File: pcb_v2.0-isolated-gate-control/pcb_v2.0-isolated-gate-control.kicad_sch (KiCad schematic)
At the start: 94 parts, among them J1 ServoLock, J10 Buttons, J11 2x encoder, J12 Screw_Terminal_01x06, J13 Relay VFD2 [NO, COM, NC], J14 GND-P, J15 Power-Servo-12V, J16 Power-LightBarrier-12V, J17 3V3 5V VDD, J18 GNDD, J2 supply, J3 12V-filtered, J4 light-barrier, reserve, J5 GND-P, J6 2x remoteControl, J7 Relay VFD1 [NO, COM, NC], J8 RS485, J9 limit, K1 RT314A24, K2 RT314A24, Q1 2N7000, Q2 2N7000, Q3 IRF5305, Q6 IRF5305, U1 esp32-devkit-v1_30Pin, U4 MAX485E, U5 L78S05CV_TO220, U6 ULN2803A

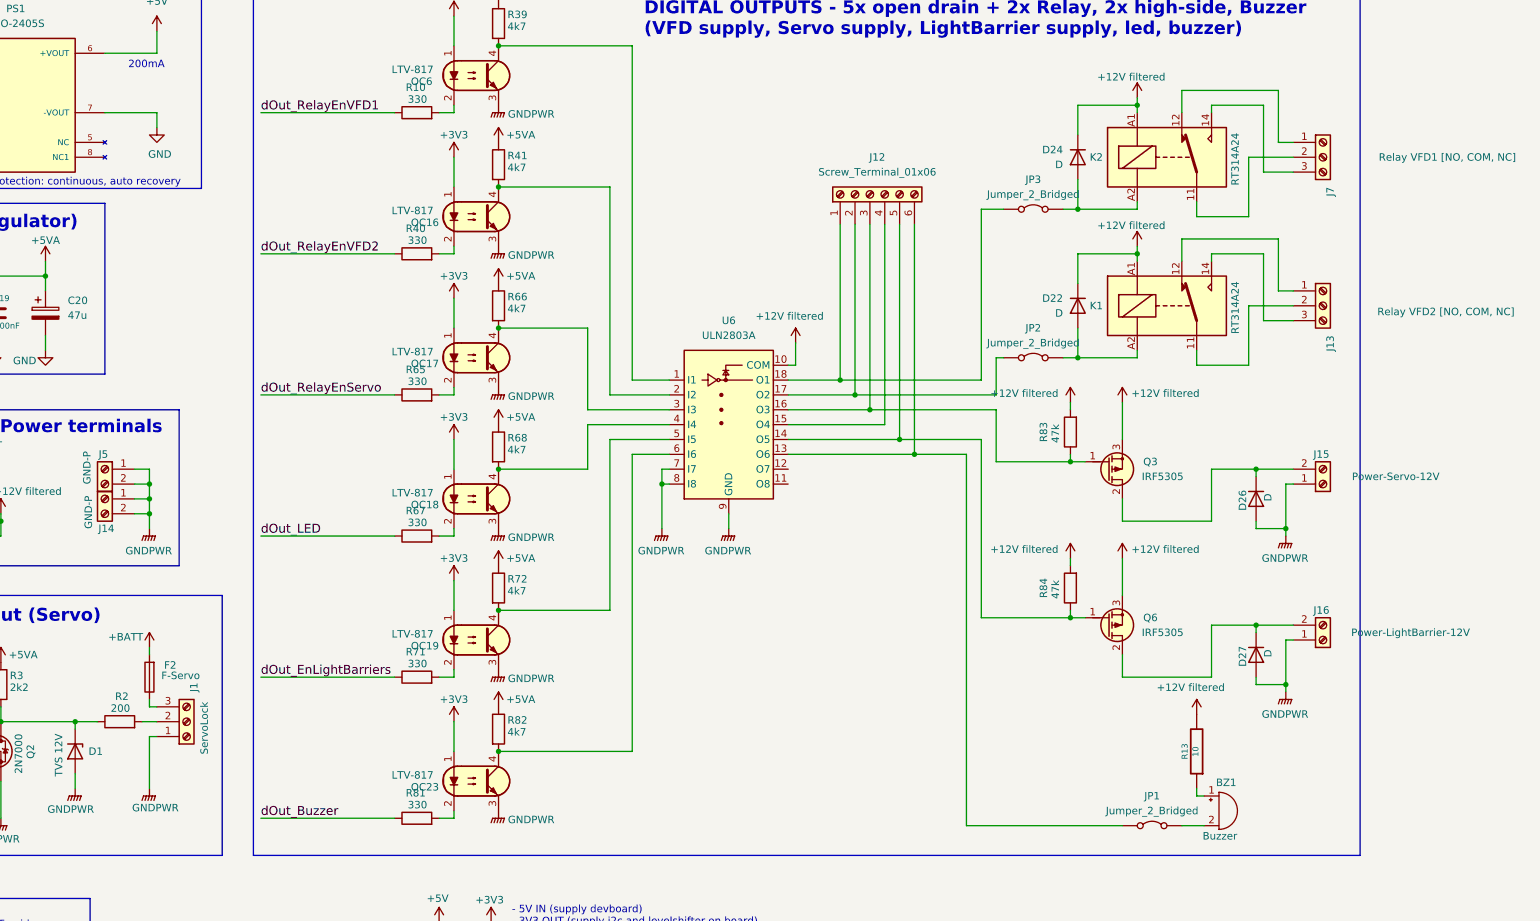
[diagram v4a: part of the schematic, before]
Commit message: pcb: arrange almost all groups inside 100x165 pcb
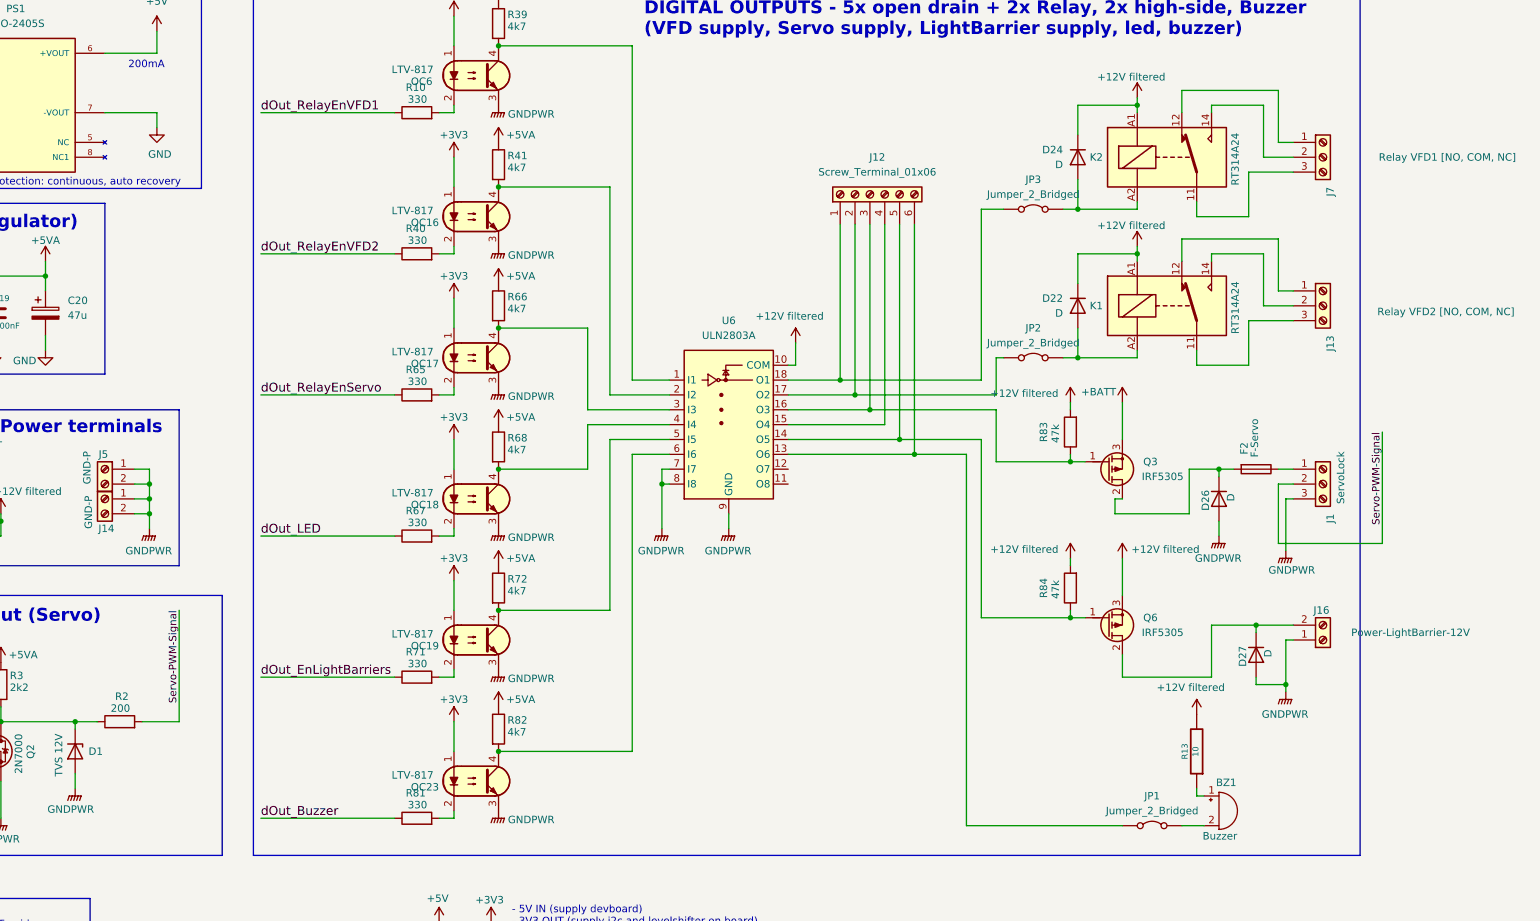
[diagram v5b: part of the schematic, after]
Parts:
- removed J15: Power-Servo-12V, TerminalBlock:TerminalBlock_bornier-2_P5.08mm, symbol Connector:Screw_Terminal_01x02
- F1, F2: footprint misc_libJonny:Fuseholder_Automotive-Regular_Fuse19x5x18mm_Footprint21x8mm_Inline -> misc_libJonny:Fuseholder_Automotive-Mini_Fuse11x4x16_Footprint15x5_Inline
- R2: footprint Resistor_THT:R_Axial_DIN0207_L6.3mm_D2.5mm_P10.16mm_Horizontal -> Resistor_THT:R_Axial_DIN0207_L6.3mm_D2.5mm_P2.54mm_Vertical
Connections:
- net +12V: no longer Q3.3 (S)
- net +BATT: now also Q3.3 (S); no longer F2.2
- net GNDPWR: now also J1.3 (Pin_3); no longer J1.1 (Pin_1)
- net at K2.11: now also J7.3 (Pin_3); no longer J7.2 (Pin_2)
- net at K2.14: now also J7.2 (Pin_2); no longer J7.3 (Pin_3)
- net at K1.11: now also J13.3 (Pin_3); no longer J13.2 (Pin_2)
- net at K1.14: now also J13.2 (Pin_2); no longer J13.3 (Pin_3)
- net at F2.1: now also J1.1 (Pin_1); no longer J1.3 (Pin_3)
- net Servo-PWM-Signal: now reaches J1.2 (Pin_2), R2.2
- net at D26.1 (K), Q3.2 (D): now also F2.2
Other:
- moved on the sheet: D26

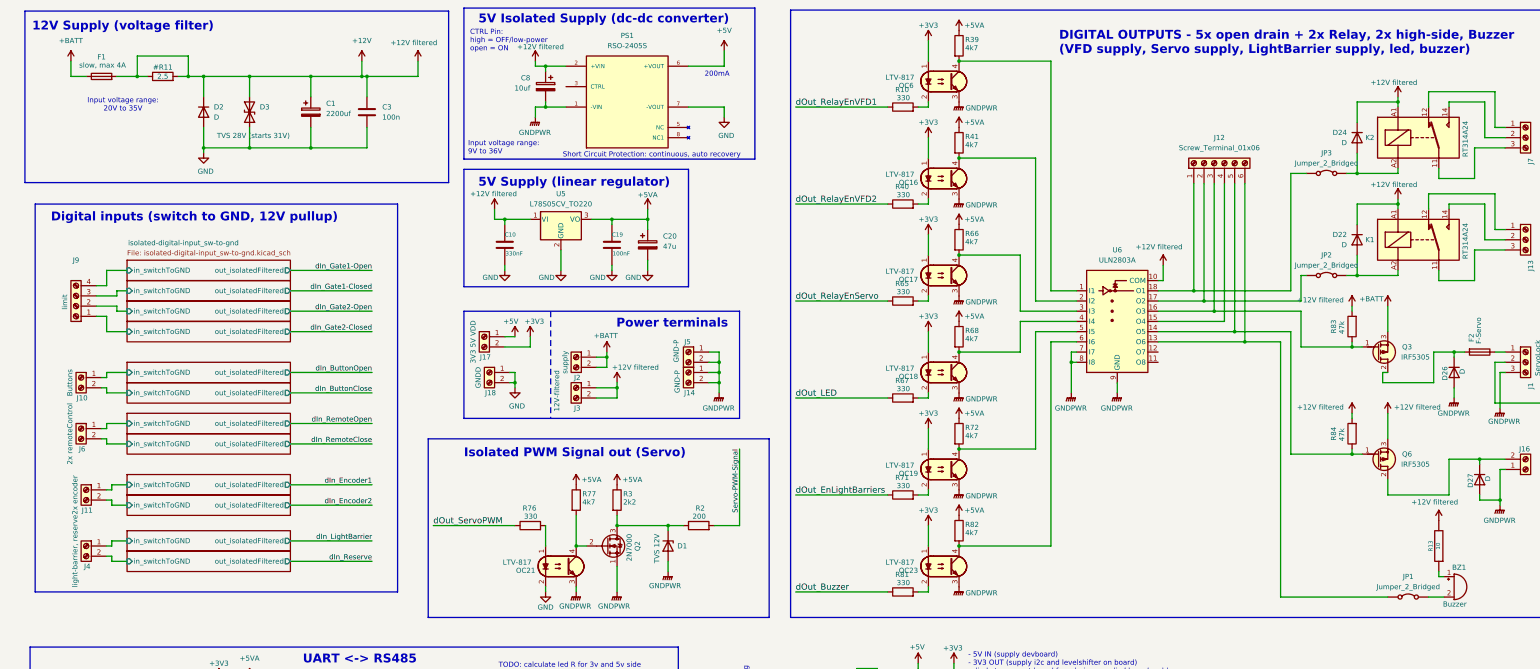
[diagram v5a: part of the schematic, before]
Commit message: pcb: Re-assign FP, Optimize arrangement, Proof-of-concept routing
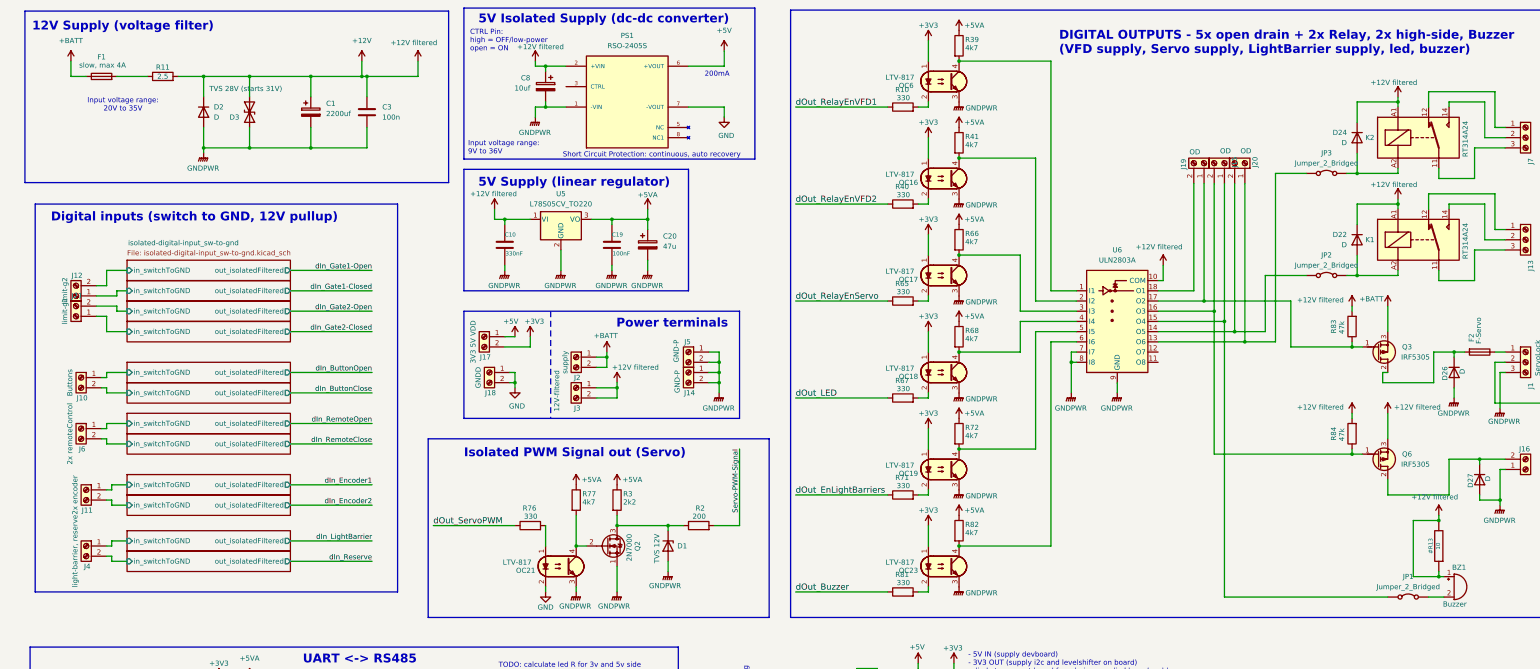
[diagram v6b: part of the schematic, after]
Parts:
- removed J12: Screw_Terminal_01x06, TerminalBlock_RND:TerminalBlock_RND_205-00016_1x06_P5.00mm_Horizontal, symbol Connector:Screw_Terminal_01x06
- removed J9: limit, TerminalBlock_Phoenix:TerminalBlock_Phoenix_MKDS-1,5-4_1x04_P5.00mm_Horizontal, symbol Connector:Screw_Terminal_01x04
- added J12: limit-g2, terminals_libJonny:ScrewTerminal_P5mm_2Pin_FP10x8, symbol Connector:Screw_Terminal_01x02
- added J15, J19, J20: OD, terminals_libJonny:ScrewTerminal_P5mm_2Pin_FP10x8, symbol Connector:Screw_Terminal_01x02
- added J21: limit-g1, terminals_libJonny:ScrewTerminal_P5mm_2Pin_FP10x8, symbol Connector:Screw_Terminal_01x02
- C1: footprint Capacitor_THT:CP_Radial_D18.0mm_P7.50mm -> Capacitor_THT:CP_Radial_D10.0mm_P3.80mm
- D1: footprint Diode_THT:D_DO-41_SOD81_P12.70mm_Horizontal -> Diode_THT:D_5W_P5.08mm_Vertical_AnodeUp
- J1, J13, J7, J8: footprint TerminalBlock:TerminalBlock_bornier-3_P5.08mm -> terminals_libJonny:ScrewTerminal_P5mm_3Pin_FP15x8
- J10, J11, J14, J16, J17, J18, J2, J3, J4, J5, J6: footprint TerminalBlock:TerminalBlock_bornier-2_P5.08mm -> terminals_libJonny:ScrewTerminal_P5mm_2Pin_FP10x8
- R11: renamed from #R11; footprint Resistor_THT:R_Axial_DIN0922_L20.0mm_D9.0mm_P25.40mm_Horizontal -> resistors_libJonny:Cement-Power-R_L22_W10_P23_Horizontal
- R3, R31, R32, R33, R34: footprint Resistor_THT:R_Axial_DIN0207_L6.3mm_D2.5mm_P10.16mm_Horizontal -> Resistor_THT:R_Axial_DIN0207_L6.3mm_D2.5mm_P2.54mm_Vertical
- renumbered R13 to #R13
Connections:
- net +12V: now also #R13.1, BZ1.1 (+), D3.1 (A1); no longer D3.2 (A2), F1.2, R11.1
- net GND: no longer C1.2, C10.2, C19.2, C20.2, C3.2, D2.2 (A), D3.1 (A1), U5.2 (GND)
- net GNDPWR: now also C1.2, C10.2, C19.2, C20.2, C3.2, D2.2 (A), D3.2 (A2), U5.2 (GND)
- net isolated-digital-input_sw-to-gnd/in_switchToGND: now also J12.2 (Pin_2)
- net isolated-digital-input_sw-to-gnd1/in_switchToGND: now also J12.1 (Pin_1)
- net isolated-digital-input_sw-to-gnd2/in_switchToGND: now also J21.2 (Pin_2)
- net isolated-digital-input_sw-to-gnd3/in_switchToGND: now also J21.1 (Pin_1)
- net at JP1.1 (A): now also U6.15 (O4), J15.1 (Pin_1); no longer U6.13 (O6)
- net at JP3.1 (A): now also U6.13 (O6), J20.1 (Pin_1); no longer U6.18 (O1)
- net at JP2.1 (A): now also U6.14 (O5), J20.2 (Pin_2); no longer U6.17 (O2)
- net at Q3.1 (G), R83.1: now also U6.17 (O2), J19.1 (Pin_1); no longer U6.16 (O3)
- net at Q6.1 (G), R84.1: now also U6.16 (O3), J15.2 (Pin_2); no longer U6.14 (O5)
- new net: F1.2, R11.1
- new net: J19.2 (Pin_2), U6.18 (O1)
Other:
- moved on the sheet: D3
